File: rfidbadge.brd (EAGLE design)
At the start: 93.7 x 48.2 mm, 57 parts, among them Q1 BSS123, U1 ATMEGA328P_TQFP, U2 CLRC663, Y1 27.12 MHz

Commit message: Some part values
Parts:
- C22, C23: value (none) -> 56 pF
- C24, C25: value (none) -> 820 pF
- R4, R5: value (none) -> 0.39
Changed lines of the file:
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@@
 </element>
 <element name="C20" library="rcl" package="C0603K" value="" x="56.515" y="34.29" rot="R270">
-<attribute name="PROD_ID" value="311-1060-1-ND" x="-28.575" y="15.24" size="1.778" layer="27" rot="R270" display="off"/>
+<attribute name="PROD_ID" value="" x="-28.575" y="15.24" size="1.778" layer="27" rot="R270" display="off"/>
 </element>
 <element name="C21" library="rcl" package="C0603K" value="" x="56.515" y="31.115" rot="R270">
-<attribute name="PROD_ID" value="311-1060-1-ND" x="-28.575" y="8.255" size="1.778" layer="27" rot="R270" display="off"/>
+<attribute name="PROD_ID" value="" x="-28.575" y="8.255" size="1.778" layer="27" rot="R270" display="off"/>
 </element>
-<element name="C22" library="rcl" package="C0603K" value="" x="59.055" y="34.29" rot="R270">
-<attribute name="PROD_ID" value="311-1060-1-ND" x="-26.035" y="7.62" size="1.778" layer="27" rot="R270" display="off"/>
+<element name="C22" library="rcl" package="C0603K" value="56 pF" x="59.055" y="34.29" rot="R270">
+<attribute name="PROD_ID" value="445-1278-1-ND" x="-26.035" y="7.62" size="1.778" layer="27" rot="R270" display="off"/>
 </element>
-<element name="C23" library="rcl" package="C0603K" value="" x="56.515" y="27.94" rot="R270">
-<attribute name="PROD_ID" value="311-1060-1-ND" x="-28.575" y="-2.54" size="1.778" layer="27" rot="R270" display="off"/>
+<element name="C23" library="rcl" package="C0603K" value="56 pF" x="56.515" y="27.94" rot="R270">
+<attribute name="PROD_ID" value="445-1278-1-ND" x="-28.575" y="-2.54" size="1.778" layer="27" rot="R270" display="off"/>
 </element>
-<element name="C24" library="rcl" package="C0603K" value="" x="59.055" y="28.8925" rot="R270">
-<attribute name="PROD_ID" value="311-1060-1-ND" x="-26.035" y="-5.3975" size="1.778" layer="27" rot="R270" display="off"/>
+<element name="C24" library="rcl" package="C0603K" value="820 pF" x="59.055" y="28.8925" rot="R270">
+<attribute name="PROD_ID" value="445-1292-1-ND" x="-26.035" y="-5.3975" size="1.778" layer="27" rot="R270" display="off"/>
 </element>
-<element name="C25" library="rcl" package="C0603K" value="" x="58.7375" y="26.3525" rot="R180">
-<attribute name="PROD_ID" value="311-1060-1-ND" x="20.6375" y="111.4425" size="1.778" layer="27" rot="R180" display="off"/>
+<element name="C25" library="rcl" package="C0603K" value="820 pF" x="58.7375" y="26.3525" rot="R180">
+<attribute name="PROD_ID" value="445-1292-1-ND" x="20.6375" y="111.4425" size="1.778" layer="27" rot="R180" display="off"/>
 </element>
-<element name="R4" library="rcl" package="R0603" value="" x="60.0075" y="31.4325"/>
-<element name="R5" library="rcl" package="R0603" value="" x="60.0075" y="21.59"/>
+<element name="R4" library="rcl" package="R0603" value="0.39" x="60.0075" y="31.4325">
+<attribute name="PROD_ID" value="P.39AHCT-ND" x="60.0075" y="31.4325" size="1.778" layer="27" display="off"/>
+</element>
+<element name="R5" library="rcl" package="R0603" value="0.39" x="60.0075" y="21.59">
+<attribute name="PROD_ID" value="P.39AHCT-ND" x="60.0075" y="21.59" size="1.778" layer="27" display="off"/>
+</element>
 <element name="ANT1" library="discrete" package="PAD-01" value="" x="62.23" y="29.21"/>
 <element name="ANT2" library="discrete" package="PAD-01" value="" x="64.897" y="24.13"/>
@@
 <element name="R7" library="rcl" package="R0603" value="" x="54.9275" y="27.94" rot="R90"/>
 <element name="C26" library="rcl" package="C0603K" value="" x="54.9275" y="37.1475">
-<attribute name="PROD_ID" value="311-1060-1-ND" x="96.8375" y="-47.9425" size="1.778" layer="27" display="off"/>
+<attribute name="PROD_ID" value="" x="96.8375" y="-47.9425" size="1.778" layer="27" display="off"/>
 </element>
 <element name="C27" library="rcl" package="C0603K" value="" x="55.5625" y="25.4" rot="R180">
-<attribute name="PROD_ID" value="311-1060-1-ND" x="9.8425" y="110.49" size="1.778" layer="27" rot="R180" display="off"/>
+<attribute name="PROD_ID" value="" x="9.8425" y="110.49" size="1.778" layer="27" rot="R180" display="off"/>
 </element>
 <element name="C28" library="rcl" package="C0603K" value="0.1 uF" x="52.07" y="33.02" rot="R270">

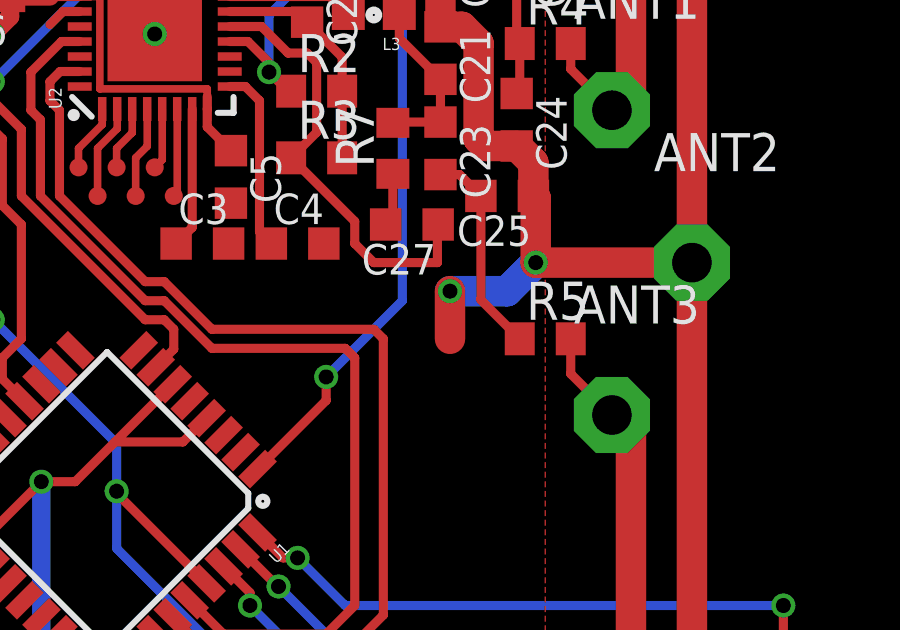
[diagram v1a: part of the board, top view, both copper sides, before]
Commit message: Values and part numbers complete
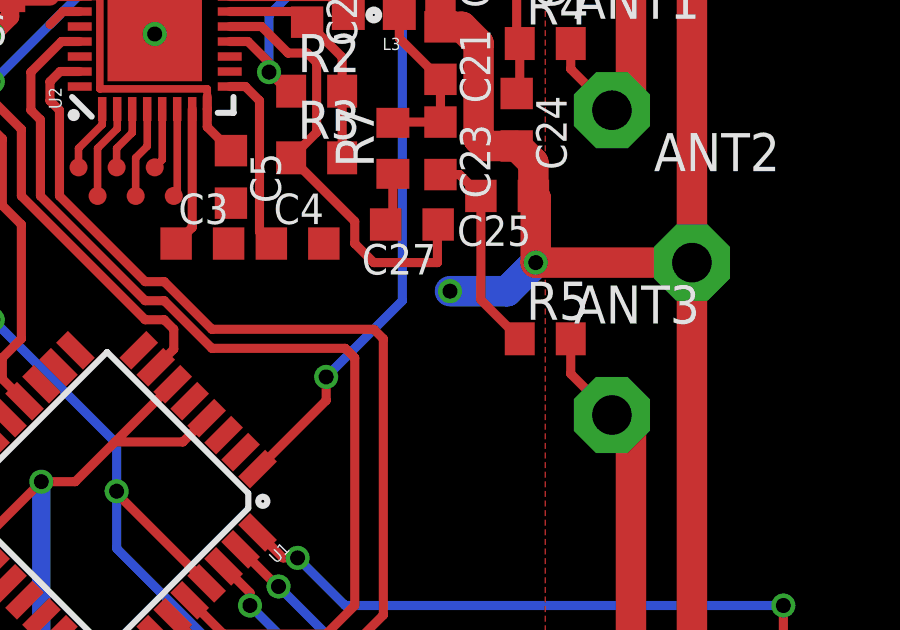
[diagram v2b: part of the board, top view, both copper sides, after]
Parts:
- C20, C21: value (none) -> 100 pF
- C26, C27: value (none) -> 1 nF
- L2, L3: value (none) -> 1.2 uH
- R6, R7: value (none) -> 15 k
- renumbered U$1 to BAT
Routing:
- net GND: track 331.9 -> 330.3 mm
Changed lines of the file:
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@@
 <attribute name="PROD_ID" value="311-1443-1-ND" x="91.44" y="-60.325" size="1.778" layer="27" display="off"/>
 </element>
-<element name="R1" library="rcl" package="R0603" value="56" x="33.655" y="40.64" rot="R90"/>
+<element name="R1" library="rcl" package="R0603" value="56" x="33.655" y="40.64" rot="R90">
+<attribute name="PROD_ID" value="P56GCT-ND" x="33.655" y="40.64" size="1.778" layer="27" rot="R90" display="off"/>
+</element>
 <element name="Q1" library="transistor-small-signal" package="SOT23" value="BSS123" x="36.83" y="39.6875" rot="R90">
 <attribute name="PROD_ID" value="2N7002ET1GOSCT-ND" x="36.83" y="39.6875" size="1.778" layer="27" rot="R90" display="off"/>
 </element>
-<element name="ISP" library="pinhead" package="2X03" value="" x="37.7825" y="2.8575"/>
-<element name="FTDI" library="pinhead" package="1X06" value="" x="50.8" y="2.54"/>
+<element name="ISP" library="pinhead" package="2X03" value="" x="37.7825" y="2.8575">
+<attribute name="PROD_ID" value="952-2121-ND" x="37.7825" y="2.8575" size="1.778" layer="27" display="off"/>
+</element>
+<element name="FTDI" library="pinhead" package="1X06" value="" x="50.8" y="2.54">
+<attribute name="PROD_ID" value="952-2270-ND" x="50.8" y="2.54" size="1.778" layer="27" display="off"/>
+</element>
 <element name="C19" library="rcl" package="C0603K" value="0.1 uF" x="56.1975" y="5.715">
 <attribute name="PROD_ID" value="311-1088-1-ND" x="110.8075" y="-70.485" size="1.778" layer="27" display="off"/>
 </element>
-<element name="R2" library="rcl" package="R0603" value="1K" x="52.3875" y="29.845"/>
-<element name="R3" library="rcl" package="R0603" value="1K" x="52.3875" y="27.6225"/>
-<element name="L2" library="SparkFun-Passives" package="0603" value="" x="54.2925" y="34.6075" rot="R180">
-<attribute name="PROD_ID" value="RES-07859" x="54.2925" y="34.6075" size="1.778" layer="27" rot="R180" display="off"/>
-</element>
-<element name="L3" library="SparkFun-Passives" package="0603" value="" x="54.2925" y="32.385" rot="R180">
-<attribute name="PROD_ID" value="RES-07859" x="54.2925" y="32.385" size="1.778" layer="27" rot="R180" display="off"/>
-</element>
-<element name="C20" library="rcl" package="C0603K" value="" x="56.515" y="34.29" rot="R270">
-<attribute name="PROD_ID" value="" x="-28.575" y="15.24" size="1.778" layer="27" rot="R270" display="off"/>
-</element>
-<element name="C21" library="rcl" package="C0603K" value="" x="56.515" y="31.115" rot="R270">
-<attribute name="PROD_ID" value="" x="-28.575" y="8.255" size="1.778" layer="27" rot="R270" display="off"/>
+<element name="R2" library="rcl" package="R0603" value="1K" x="52.3875" y="29.845">
+<attribute name="PROD_ID" value="P1.0KGCT-ND" x="52.3875" y="29.845" size="1.778" layer="27" display="off"/>
+</element>
+<element name="R3" library="rcl" package="R0603" value="1K" x="52.3875" y="27.6225">
+<attribute name="PROD_ID" value="P1.0KGCT-ND" x="52.3875" y="27.6225" size="1.778" layer="27" display="off"/>
+</element>
+<element name="L2" library="SparkFun-Passives" package="0603" value="1.2 uH" x="54.2925" y="34.6075" rot="R180">
+<attribute name="PROD_ID" value="535-12527-1-ND" x="54.2925" y="34.6075" size="1.778" layer="27" rot="R180" display="off"/>
+</element>
+<element name="L3" library="SparkFun-Passives" package="0603" value="1.2 uH" x="54.2925" y="32.385" rot="R180">
+<attribute name="PROD_ID" value="535-12527-1-ND" x="54.2925" y="32.385" size="1.778" layer="27" rot="R180" display="off"/>
+</element>
+<element name="C20" library="rcl" package="C0603K" value="100 pF" x="56.515" y="34.29" rot="R270">
+<attribute name="PROD_ID" value="311-1069-1-ND" x="-28.575" y="15.24" size="1.778" layer="27" rot="R270" display="off"/>
+</element>
+<element name="C21" library="rcl" package="C0603K" value="100 pF" x="56.515" y="31.115" rot="R270">
+<attribute name="PROD_ID" value="311-1069-1-ND" x="-28.575" y="8.255" size="1.778" layer="27" rot="R270" display="off"/>
 </element>
 <element name="C22" library="rcl" package="C0603K" value="56 pF" x="59.055" y="34.29" rot="R270">
@@
 <element name="ANT2" library="discrete" package="PAD-01" value="" x="64.897" y="24.13"/>
 <element name="ANT3" library="discrete" package="PAD-01" value="" x="62.23" y="19.05"/>
-<element name="R6" library="rcl" package="R0603" value="" x="58.1025" y="37.1475" rot="R180"/>
-<element name="R7" library="rcl" package="R0603" value="" x="54.9275" y="27.94" rot="R90"/>
-<element name="C26" library="rcl" package="C0603K" value="" x="54.9275" y="37.1475">
-<attribute name="PROD_ID" value="" x="96.8375" y="-47.9425" size="1.778" layer="27" display="off"/>
-</element>
-<element name="C27" library="rcl" package="C0603K" value="" x="55.5625" y="25.4" rot="R180">
-<attribute name="PROD_ID" value="" x="9.8425" y="110.49" size="1.778" layer="27" rot="R180" display="off"/>
+<element name="R6" library="rcl" package="R0603" value="15 k" x="58.1025" y="37.1475" rot="R180">
+<attribute name="PROD_ID" value="P15KGCT-ND" x="58.1025" y="37.1475" size="1.778" layer="27" rot="R180" display="off"/>
+</element>
+<element name="R7" library="rcl" package="R0603" value="15 k" x="54.9275" y="27.94" rot="R90">
+<attribute name="PROD_ID" value="P15KGCT-ND" x="54.9275" y="27.94" size="1.778" layer="27" rot="R90" display="off"/>
+</element>
+<element name="C26" library="rcl" package="C0603K" value="1 nF" x="54.9275" y="37.1475">
+<attribute name="PROD_ID" value="311-1342-1-ND" x="96.8375" y="-47.9425" size="1.778" layer="27" display="off"/>
+</element>
+<element name="C27" library="rcl" package="C0603K" value="1 nF" x="55.5625" y="25.4" rot="R180">
+<attribute name="PROD_ID" value="311-1342-1-ND" x="9.8425" y="110.49" size="1.778" layer="27" rot="R180" display="off"/>
 </element>
 <element name="C28" library="rcl" package="C0603K" value="0.1 uF" x="52.07" y="33.02" rot="R270">
 <attribute name="PROD_ID" value="311-1088-1-ND" x="-33.02" y="-16.51" size="1.778" layer="27" rot="R270" display="off"/>
 </element>
-<element name="U$1" library="battery_holder" package="AAA_X3" value="AAA_X3" x="30.48" y="24.13" rot="MR0">
+<element name="BAT" library="battery_holder" package="AAA_X3" value="AAA_X3" x="30.48" y="24.13" rot="MR0">
 <attribute name="PROD_ID" value="36-2479-ND" x="30.48" y="24.13" size="1.778" layer="28" rot="MR0" display="off"/>
 </element>
@@
 <contactref element="FTDI" pad="1"/>
 <contactref element="FTDI" pad="2"/>
-<contactref element="U$1" pad="NEG"/>
+<contactref element="BAT" pad="NEG"/>
 <wire x1="56.43" y1="33.5" x2="56.515" y2="33.415" width="0.3048" layer="1"/>
 <wire x1="56.515" y1="33.415" x2="56.515" y2="31.99" width="1.016" layer="1"/>
@@
 <wire x1="58.7375" y1="23.1775" x2="56.8325" y2="23.1775" width="1.016" layer="16"/>
 <via x="56.8325" y="23.1775" extent="1-16" drill="0.5"/>
-<wire x1="56.8325" y1="23.1775" x2="56.8325" y2="21.59" width="1.016" layer="1"/>
+<wire x1="56.8325" y1="23.1775" x2="56.8325" y2="21.59" width="0" layer="19" extent="1-16"/>
 <wire x1="59.6125" y1="26.3525" x2="59.69" y2="26.275" width="1.016" layer="1"/>
 <wire x1="59.69" y1="26.275" x2="59.69" y2="24.13" width="1.016" layer="1"/>
@@
 <contactref element="LCD" pad="A"/>
 <contactref element="ISP" pad="2"/>
-<contactref element="U$1" pad="POS"/>
+<contactref element="BAT" pad="POS"/>
 <contactref element="U2" pad="25"/>
 <contactref element="C6" pad="1"/>

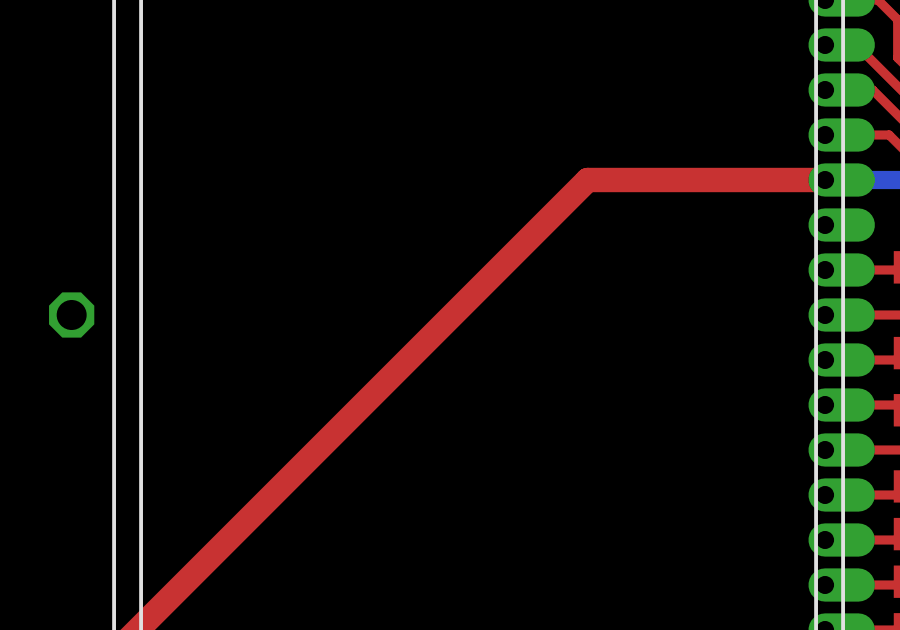
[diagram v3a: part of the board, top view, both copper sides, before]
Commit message: Fix orphaned ground plane
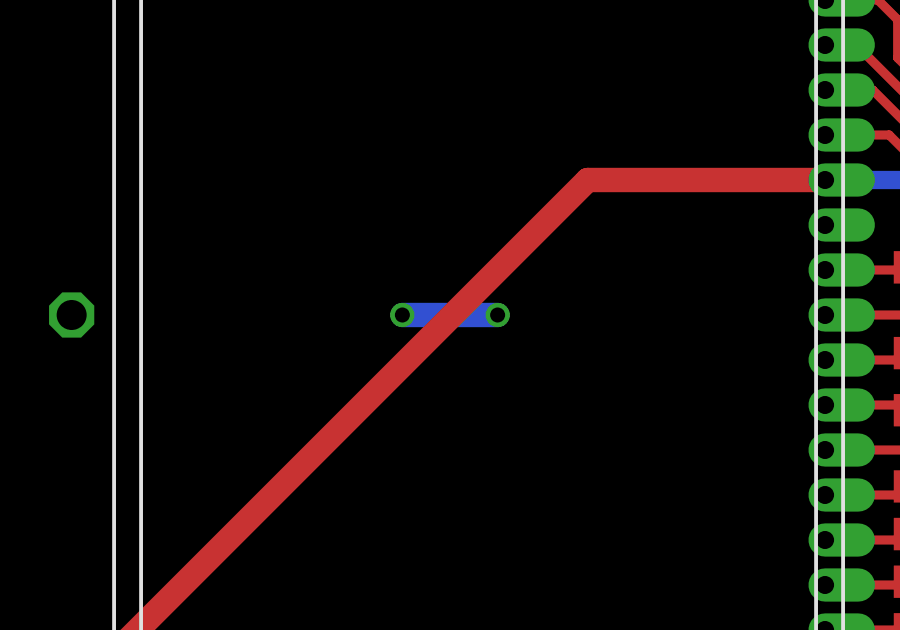
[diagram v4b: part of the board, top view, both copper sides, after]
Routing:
- net GND: track 330.3 -> 333.5 mm, vias 10 -> 12
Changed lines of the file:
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@@
 <wire x1="58.7375" y1="23.1775" x2="56.8325" y2="23.1775" width="1.016" layer="16"/>
 <via x="56.8325" y="23.1775" extent="1-16" drill="0.5"/>
-<wire x1="56.8325" y1="23.1775" x2="56.8325" y2="21.59" width="0" layer="19" extent="1-16"/>
 <wire x1="59.6125" y1="26.3525" x2="59.69" y2="26.275" width="1.016" layer="1"/>
 <wire x1="59.69" y1="26.275" x2="59.69" y2="24.13" width="1.016" layer="1"/>
@@
 <wire x1="67.945" y1="8.5725" x2="59.3725" y2="8.5725" width="0.3048" layer="16"/>
 <via x="59.3725" y="8.5725" extent="1-16" drill="0.5"/>
-<wire x1="42.650015625" y1="12.874328125" x2="36.435" y2="12.065" width="0" layer="19" extent="1-1"/>
+<via x="20.955" y="24.13" extent="1-16" drill="0.5"/>
+<wire x1="20.955" y1="24.13" x2="17.78" y2="24.13" width="0.8128" layer="16"/>
+<via x="17.78" y="24.13" extent="1-16" drill="0.5"/>
 </signal>
 <signal name="EXTCLK">

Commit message: s/CLRC633/CLRC663/
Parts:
- U2: device CLRC633:QFN32 -> CLRC663:QFN32
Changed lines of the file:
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@@
 <attribute name="PROD_ID" value="ATMEGA328PB-AURCT-ND" x="-30.03165" y="5.41619375" size="1.778" layer="27" rot="R225" display="off"/>
 </element>
-<element name="U2" library="CLRC633" package="QFN32" value="CLRC663" x="46.99" y="31.75" rot="R90">
+<element name="U2" library="CLRC663" package="QFN32" value="CLRC663" x="46.99" y="31.75" rot="R90">
 <attribute name="PROD_ID" value="568-11528-ND" x="116.84" y="57.15" size="1.778" layer="27" rot="R90" display="off"/>
 </element>
